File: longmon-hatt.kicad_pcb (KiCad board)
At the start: 2 copper layers, 2 parts

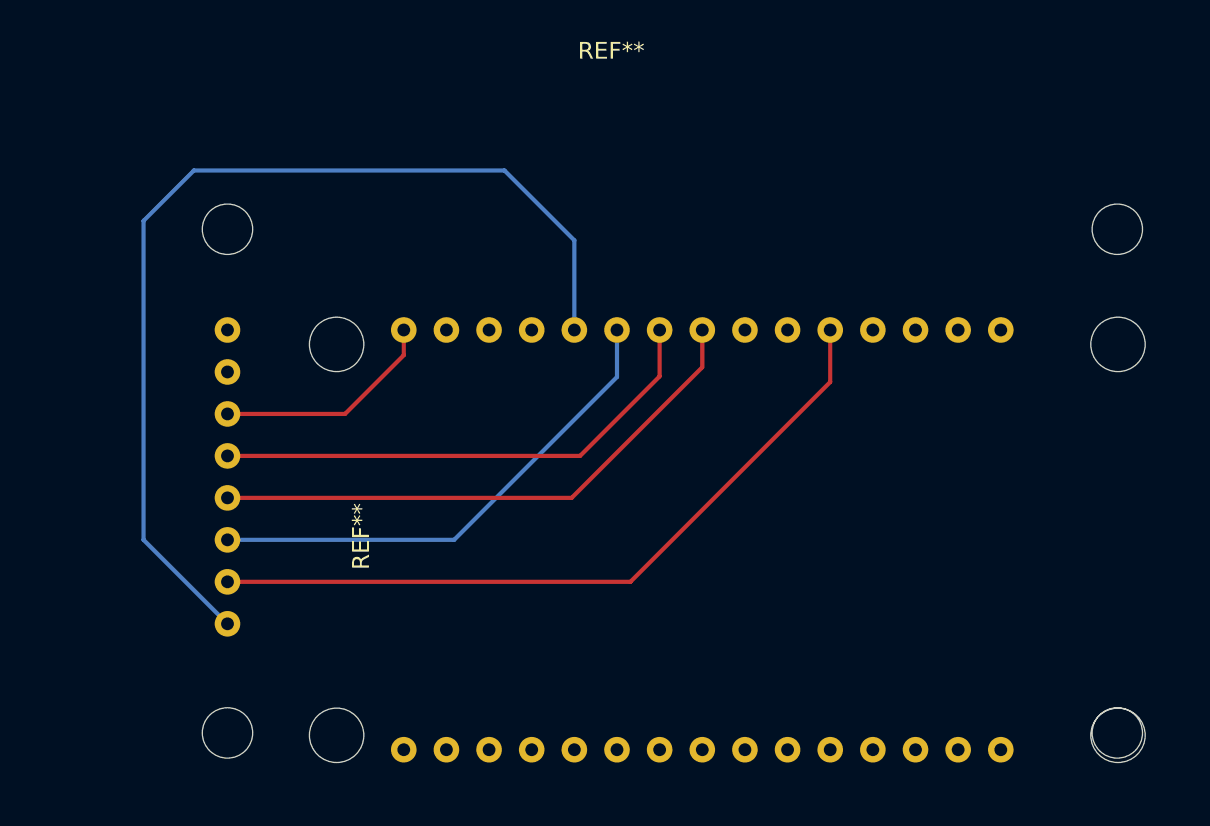
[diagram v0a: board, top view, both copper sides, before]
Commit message: Fixed pad numbers on ESP footprint, fix ref designators on PCB
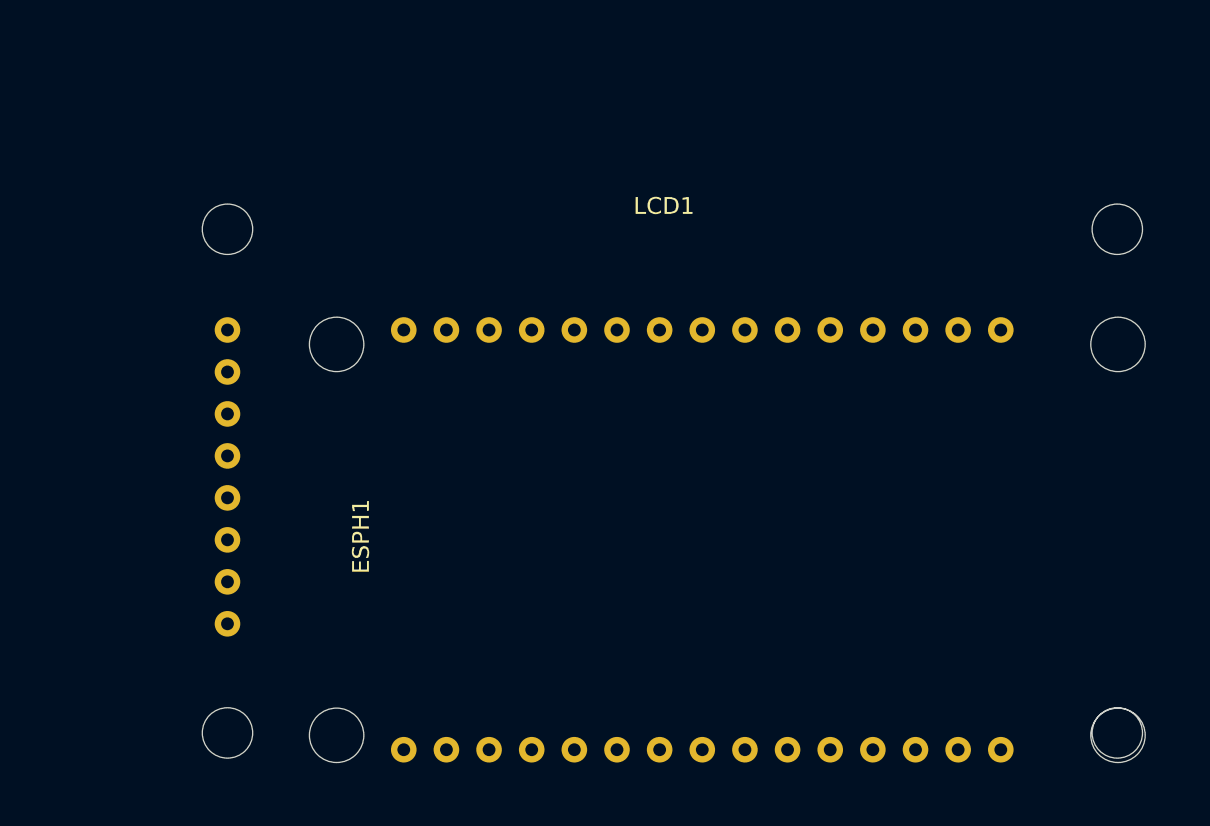
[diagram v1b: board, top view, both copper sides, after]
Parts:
- ESPH1: renamed from REF**; value ESP_Header -> ~
- LCD1: renamed from REF**; value LCD Module -> ~
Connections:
- ESPH1 pad 10: (no net) -> Net-(ESPH1-D34)
- ESPH1 pad 11: (no net) -> unconnected-(ESPH1-D35-Pad11)
- ESPH1 pad 12: (no net) -> unconnected-(ESPH1-D32-Pad12)
- ESPH1 pad 13: (no net) -> unconnected-(ESPH1-D33-Pad13)
- ESPH1 pad 14: (no net) -> unconnected-(ESPH1-D25-Pad14)
- ESPH1 pad 15: (no net) -> unconnected-(ESPH1-D26-Pad15)
- ESPH1 pad 16: (no net) -> unconnected-(ESPH1-D27-Pad16)
- ESPH1 pad 17: (no net) -> unconnected-(ESPH1-D14-Pad17)
- ESPH1 pad 18: (no net) -> unconnected-(ESPH1-D12-Pad18)
- ESPH1 pad 20: (no net) -> unconnected-(ESPH1-D13-Pad20)
- ESPH1 pad 21: (no net) -> unconnected-(ESPH1-D15-Pad21)
- ESPH1 pad 22: (no net) -> unconnected-(ESPH1-D2-Pad22)
- ESPH1 pad 24: (no net) -> Net-(ESPH1-D4)
- ESPH1 pad 25: (no net) -> Net-(ESPH1-RX2)
- ESPH1 pad 27: (no net) -> Net-(ESPH1-TX2)
- ESPH1 pad 5: (no net) -> unconnected-(ESPH1-VP-Pad5)
- ESPH1 pad 8: (no net) -> unconnected-(ESPH1-VN-Pad8)
- ESPH1 pad 9: (no net) -> unconnected-(ESPH1-EN-Pad9)
- LCD1 pad 1: (no net) -> Net-(LCD1-VCC)
- LCD1 pad 2: (no net) -> Net-(LCD1-GND)
- LCD1 pad 3: (no net) -> Net-(ESPH1-D23)
- LCD1 pad 4: (no net) -> Net-(ESPH1-D18)
- LCD1 pad 5: (no net) -> Net-(ESPH1-D5)
- LCD1 pad 6: (no net) -> Net-(ESPH1-D19)
- LCD1 pad 7: (no net) -> Net-(ESPH1-D4)
- LCD1 pad 8: (no net) -> Net-(ESPH1-D21)
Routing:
- net (no net): track 211.6 -> 0.00 mm

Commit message: Add LoRa header (TODO: fix pin order), add edge cut
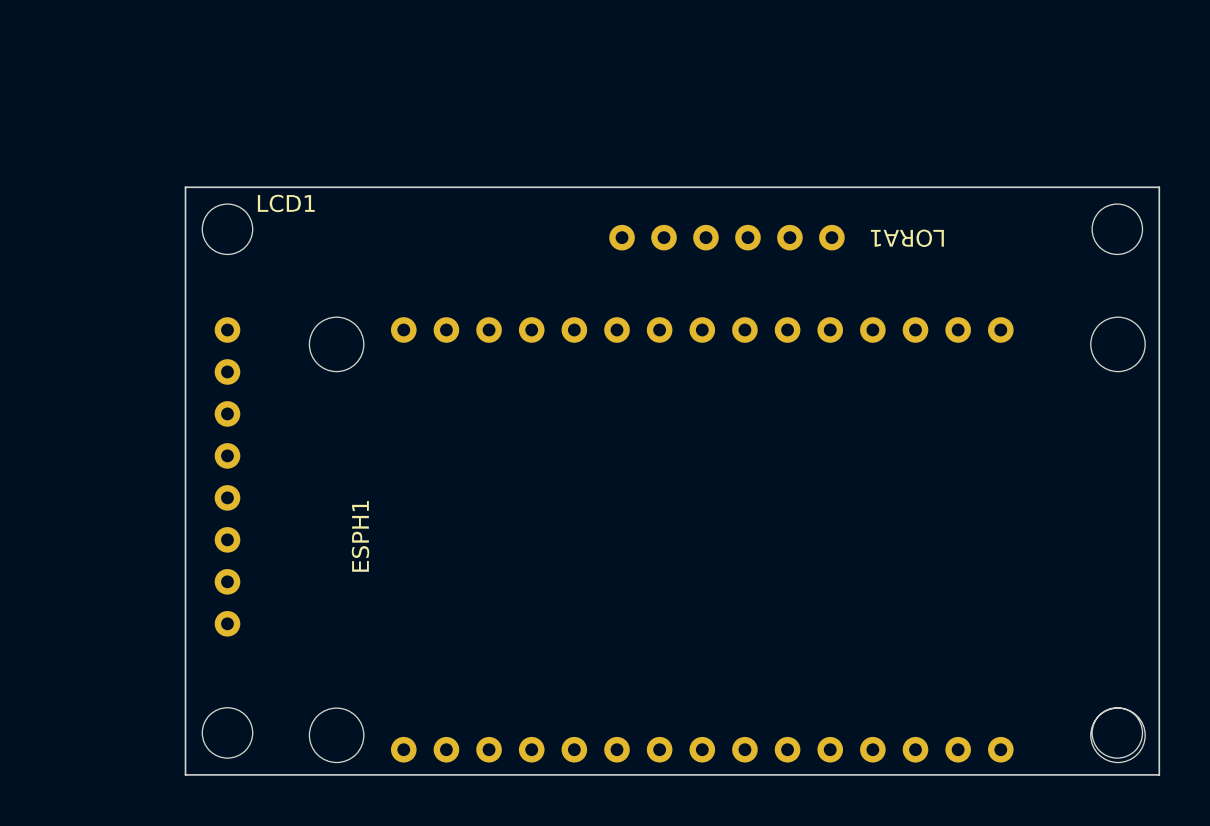
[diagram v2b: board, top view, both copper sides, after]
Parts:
- added LORA1: ~, ESP:LoRa Header, F.Cu at (175.5, 82.0)
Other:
- board outline added: 58 x 35 mm
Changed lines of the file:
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@@
     )
     (pad_to_mask_clearance 0)
+    (aux_axis_origin 166 96.5)
     (pcbplotparams
       (layerselection 0x00010fc_ffffffff)
@@
   (net 28 "Net-(LCD1-GND)")
   (net 29 "Net-(ESPH1-PadVIN)")
+  (net 30 "unconnected-(LORA1-NRST-Pad4)")
   (footprint "ESP:ESP_Header" (layer "F.Cu")
     (at 150 112.5 90)
@@
         (effects (font (size 1 1) (thickness 0.1)))
     )
-    (fp_text value "~" (at 12.7 0 90 unlocked) (layer "F.Fab")
+    (fp_text value "~" (at 12.7 0 90 unlocked) (layer "F.Fab") hide
         (effects (font (size 1 1) (thickness 0.15)))
     )
@@
       (net 29 "Net-(ESPH1-PadVIN)") (pinfunction "VIN") (pintype "power_in"))
   )
+  (footprint "ESP:LoRa Header" (layer "F.Cu")
+    (at 175.5 82 -90)
+    (property "Sheetfile" "longmon-hatt.kicad_sch")
+    (property "Sheetname" "")
+    (property "Sim.Enable" "0")
+    (attr through_hole)
+    (fp_text reference "LORA1" (at 0 -4.5 -180 unlocked) (layer "F.SilkS")
+        (effects (font (size 1 1) (thickness 0.1)))
+    )
+    (fp_text value "~" (at 12.5 -5 -90 unlocked) (layer "F.Fab") hide
+        (effects (font (size 1 1) (thickness 0.15)))
+    )
+    (fp_text user "${REFERENCE}" (at 12.5 -3.5 -90 unlocked) (layer "F.Fab") hide
+        (effects (font (size 1 1) (thickness 0.15)))
+    )
+    (pad "1" thru_hole circle (at 0 0 270) (size 1.524 1.524) (drill 0.762) (layers "*.Cu" "*.Mask")
+      (net 28 "Net-(LCD1-GND)") (pinfunction "GND") (pintype "power_in"))
+    (pad "2" thru_hole circle (at 0 2.5 270) (size 1.524 1.524) (drill 0.762) (layers "*.Cu" "*.Mask")
+      (net 18 "Net-(ESPH1-RX2)") (pinfunction "TXD") (pintype "output"))
+    (pad "3" thru_hole circle (at 0 5 270) (size 1.524 1.524) (drill 0.762) (layers "*.Cu" "*.Mask")
+      (net 19 "Net-(ESPH1-TX2)") (pinfunction "RXD") (pintype "input"))
+    (pad "4" thru_hole circle (at 0 7.5 270) (size 1.524 1.524) (drill 0.762) (layers "*.Cu" "*.Mask")
+      (net 30 "unconnected-(LORA1-NRST-Pad4)") (pinfunction "NRST") (pintype "no_connect"))
+    (pad "5" thru_hole circle (at 0 10 270) (size 1.524 1.524) (drill 0.762) (layers "*.Cu" "*.Mask")
+      (net 1 "Net-(LCD1-VCC)") (pinfunction "VDD") (pintype "power_in"))
+    (pad "6" thru_hole circle (at 0 12.5 270) (size 1.524 1.524) (drill 0.762) (layers "*.Cu" "*.Mask"))
+  )
   (footprint "ESP:LCD Module" (layer "F.Cu")
     (at 139.5 81.5)
@@
     (property "Sim.Enable" "0")
     (attr through_hole)
-    (fp_text reference "LCD1" (at 26 -1.38 unlocked) (layer "F.SilkS")
+    (fp_text reference "LCD1" (at 3.5 -1.5 unlocked) (layer "F.SilkS")
         (effects (font (size 1 1) (thickness 0.1)))
     )
-    (fp_text value "~" (at 26 0.5 unlocked) (layer "F.Fab")
+    (fp_text value "~" (at 26 0.5 unlocked) (layer "F.Fab") hide
         (effects (font (size 1 1) (thickness 0.15)))
     )
@@
       (net 27 "Net-(ESPH1-D21)") (pinfunction "BL") (pintype "input"))
   )
+  (gr_rect (start 137 79) (end 195 114)
+    (stroke (width 0.1) (type default)) (fill none) (layer "Edge.Cuts"))
 )

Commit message: Fix LoRa pins and pads, add design constraints
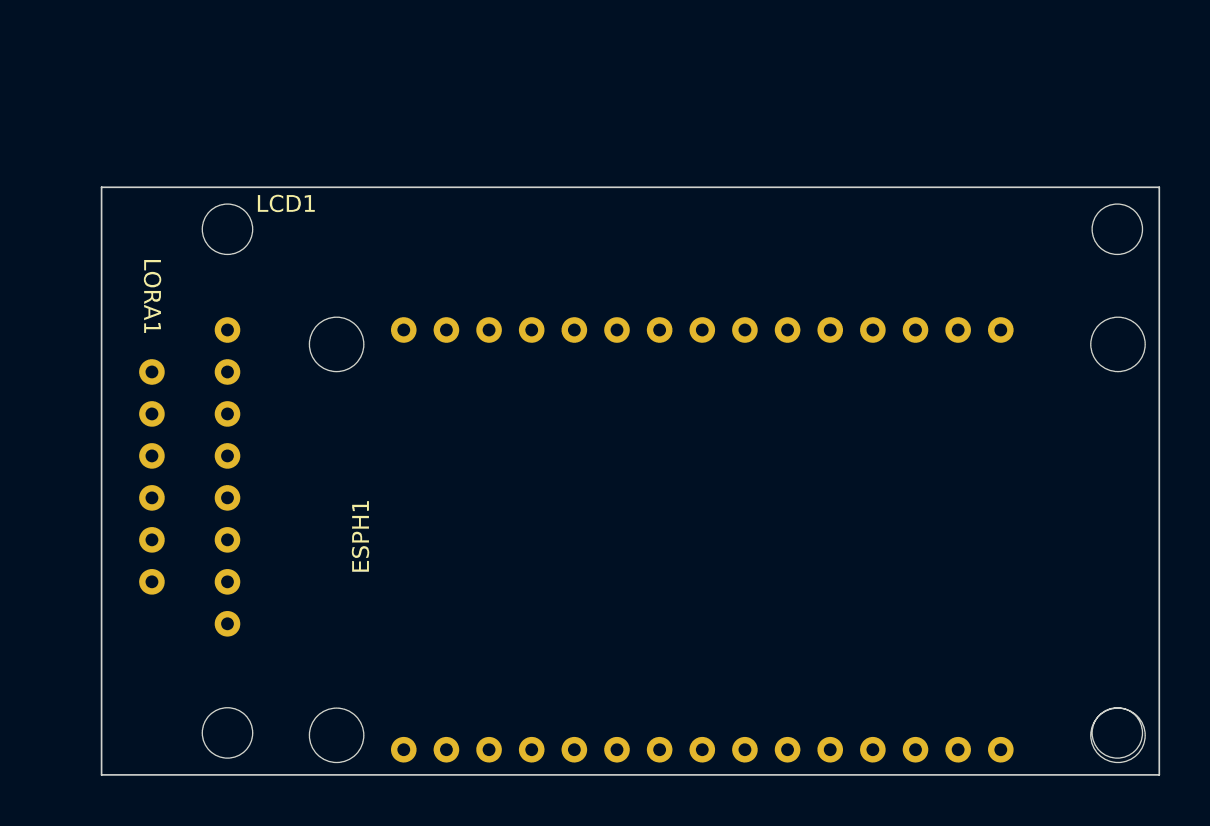
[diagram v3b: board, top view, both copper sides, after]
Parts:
- moved LORA1 41.3 mm to (135.0, 90.0), turned to 0 degrees
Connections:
- LORA1 pad 2: Net-(ESPH1-RX2) -> (no net)
- LORA1 pad 3: Net-(ESPH1-TX2) -> Net-(ESPH1-RX2)
- LORA1 pad 4: unconnected-(LORA1-NRST-Pad4) -> Net-(ESPH1-TX2)
- LORA1 pad 5: Net-(LCD1-VCC) -> unconnected-(LORA1-NRST-Pad5)
- LORA1 pad 6: (no net) -> Net-(LCD1-VCC)
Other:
- board size 58 x 35 mm -> 63 x 35 mm
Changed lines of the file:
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@@
   (net 28 "Net-(LCD1-GND)")
   (net 29 "Net-(ESPH1-PadVIN)")
-  (net 30 "unconnected-(LORA1-NRST-Pad4)")
+  (net 30 "unconnected-(LORA1-NRST-Pad5)")
   (footprint "ESP:ESP_Header" (layer "F.Cu")
     (at 150 112.5 90)
@@
   )
   (footprint "ESP:LoRa Header" (layer "F.Cu")
-    (at 175.5 82 -90)
+    (at 135 90)
     (property "Sheetfile" "longmon-hatt.kicad_sch")
     (property "Sheetname" "")
     (property "Sim.Enable" "0")
     (attr through_hole)
-    (fp_text reference "LORA1" (at 0 -4.5 -180 unlocked) (layer "F.SilkS")
+    (fp_text reference "LORA1" (at 0 -4.5 -90 unlocked) (layer "F.SilkS")
         (effects (font (size 1 1) (thickness 0.1)))
     )
-    (fp_text value "~" (at 12.5 -5 -90 unlocked) (layer "F.Fab") hide
+    (fp_text value "~" (at 12.5 -5 unlocked) (layer "F.Fab") hide
         (effects (font (size 1 1) (thickness 0.15)))
     )
-    (fp_text user "${REFERENCE}" (at 12.5 -3.5 -90 unlocked) (layer "F.Fab") hide
+    (fp_text user "${REFERENCE}" (at 12.5 -3.5 unlocked) (layer "F.Fab") hide
         (effects (font (size 1 1) (thickness 0.15)))
     )
-    (pad "1" thru_hole circle (at 0 0 270) (size 1.524 1.524) (drill 0.762) (layers "*.Cu" "*.Mask")
+    (pad "1" thru_hole circle (at 0 0) (size 1.524 1.524) (drill 0.762) (layers "*.Cu" "*.Mask")
       (net 28 "Net-(LCD1-GND)") (pinfunction "GND") (pintype "power_in"))
-    (pad "2" thru_hole circle (at 0 2.5 270) (size 1.524 1.524) (drill 0.762) (layers "*.Cu" "*.Mask")
+    (pad "2" thru_hole circle (at 0 2.5) (size 1.524 1.524) (drill 0.762) (layers "*.Cu" "*.Mask"))
+    (pad "3" thru_hole circle (at 0 5) (size 1.524 1.524) (drill 0.762) (layers "*.Cu" "*.Mask")
       (net 18 "Net-(ESPH1-RX2)") (pinfunction "TXD") (pintype "output"))
-    (pad "3" thru_hole circle (at 0 5 270) (size 1.524 1.524) (drill 0.762) (layers "*.Cu" "*.Mask")
+    (pad "4" thru_hole circle (at 0 7.5) (size 1.524 1.524) (drill 0.762) (layers "*.Cu" "*.Mask")
       (net 19 "Net-(ESPH1-TX2)") (pinfunction "RXD") (pintype "input"))
-    (pad "4" thru_hole circle (at 0 7.5 270) (size 1.524 1.524) (drill 0.762) (layers "*.Cu" "*.Mask")
-      (net 30 "unconnected-(LORA1-NRST-Pad4)") (pinfunction "NRST") (pintype "no_connect"))
-    (pad "5" thru_hole circle (at 0 10 270) (size 1.524 1.524) (drill 0.762) (layers "*.Cu" "*.Mask")
+    (pad "5" thru_hole circle (at 0 10) (size 1.524 1.524) (drill 0.762) (layers "*.Cu" "*.Mask")
+      (net 30 "unconnected-(LORA1-NRST-Pad5)") (pinfunction "NRST") (pintype "no_connect"))
+    (pad "6" thru_hole circle (at 0 12.5) (size 1.524 1.524) (drill 0.762) (layers "*.Cu" "*.Mask")
       (net 1 "Net-(LCD1-VCC)") (pinfunction "VDD") (pintype "power_in"))
-    (pad "6" thru_hole circle (at 0 12.5 270) (size 1.524 1.524) (drill 0.762) (layers "*.Cu" "*.Mask"))
   )
   (footprint "ESP:LCD Module" (layer "F.Cu")
@@
       (net 27 "Net-(ESPH1-D21)") (pinfunction "BL") (pintype "input"))
   )
-  (gr_rect (start 137 79) (end 195 114)
+  (gr_rect (start 132 79) (end 195 114)
     (stroke (width 0.1) (type default)) (fill none) (layer "Edge.Cuts"))
 )

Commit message: Add POT header
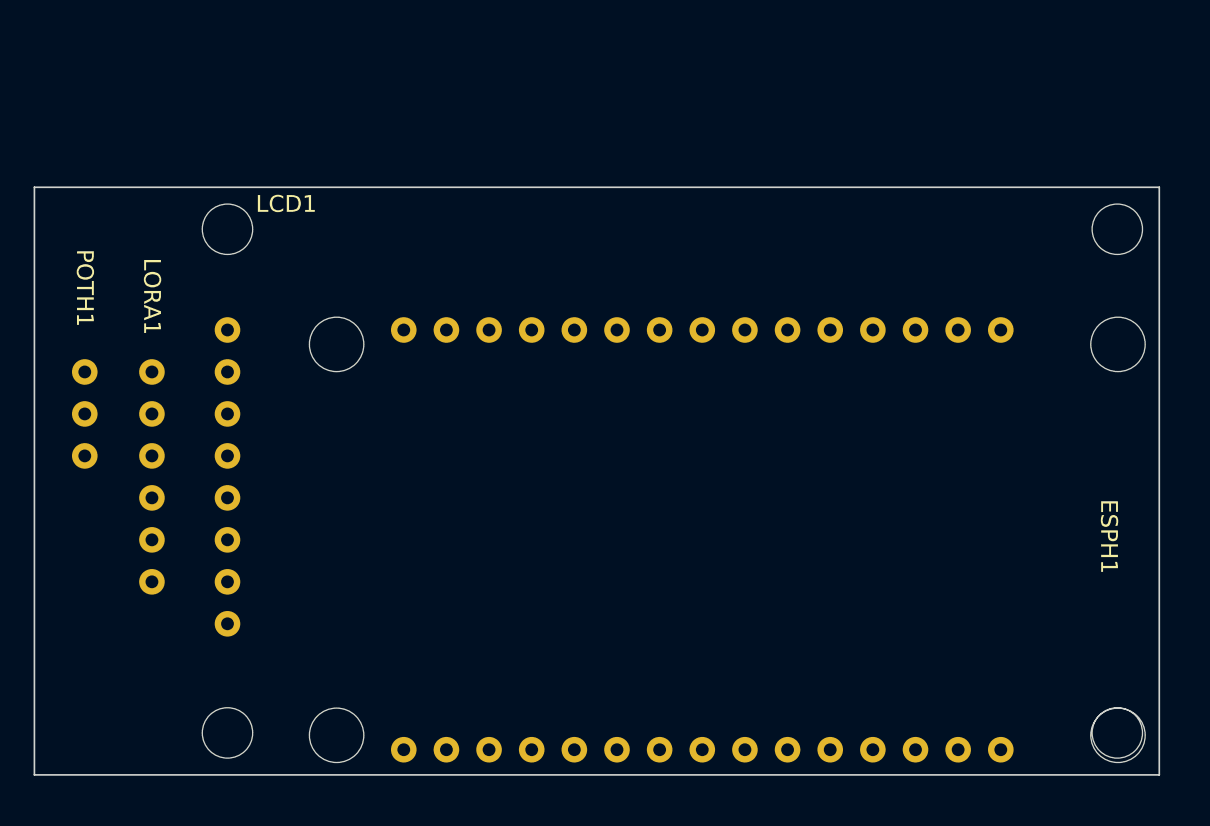
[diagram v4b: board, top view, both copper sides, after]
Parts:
- added POTH1: ~, ESP:POT Header, F.Cu at (131.0, 90.0)
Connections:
- ESPH1 pad VIN: Net-(ESPH1-PadVIN) -> unconnected-(ESPH1-PadVIN)
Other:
- board size 63 x 35 mm -> 67 x 35 mm
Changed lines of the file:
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@@
   (net 27 "Net-(ESPH1-D21)")
   (net 28 "Net-(LCD1-GND)")
-  (net 29 "Net-(ESPH1-PadVIN)")
+  (net 29 "unconnected-(ESPH1-PadVIN)")
   (net 30 "unconnected-(LORA1-NRST-Pad5)")
   (footprint "ESP:ESP_Header" (layer "F.Cu")
@@
     (property "ki_keywords" "ESP, header")
     (attr through_hole)
-    (fp_text reference "ESPH1" (at 12.7 -2.54 90 unlocked) (layer "F.SilkS")
+    (fp_text reference "ESPH1" (at 12.7 42 270 unlocked) (layer "F.SilkS")
         (effects (font (size 1 1) (thickness 0.1)))
     )
@@
       (net 28 "Net-(LCD1-GND)") (pinfunction "GND") (pintype "power_in"))
     (pad "VIN" thru_hole circle (at 0 35.56 90) (size 1.524 1.524) (drill 0.762) (layers "*.Cu" "*.Mask")
-      (net 29 "Net-(ESPH1-PadVIN)") (pinfunction "VIN") (pintype "power_in"))
+      (net 29 "unconnected-(ESPH1-PadVIN)") (pinfunction "VIN") (pintype "power_in"))
   )
   (footprint "ESP:LoRa Header" (layer "F.Cu")
@@
       (net 1 "Net-(LCD1-VCC)") (pinfunction "VDD") (pintype "power_in"))
   )
+  (footprint "ESP:POT Header" (layer "F.Cu")
+    (at 131 90)
+    (property "Sheetfile" "longmon-hatt.kicad_sch")
+    (property "Sheetname" "")
+    (property "Sim.Enable" "0")
+    (attr through_hole)
+    (fp_text reference "POTH1" (at 0 -5 -90 unlocked) (layer "F.SilkS")
+        (effects (font (size 1 1) (thickness 0.1)))
+    )
+    (fp_text value "~" (at 7.5 1.5 unlocked) (layer "F.Fab") hide
+        (effects (font (size 1 1) (thickness 0.15)))
+    )
+    (fp_text user "${REFERENCE}" (at 7.5 3 unlocked) (layer "F.Fab") hide
+        (effects (font (size 1 1) (thickness 0.15)))
+    )
+    (pad "DIV" thru_hole circle (at 0 2.5) (size 1.524 1.524) (drill 0.762) (layers "*.Cu" "*.Mask")
+      (net 5 "Net-(ESPH1-D34)") (pinfunction "DIV") (pintype "output"))
+    (pad "GND" thru_hole circle (at 0 5) (size 1.524 1.524) (drill 0.762) (layers "*.Cu" "*.Mask")
+      (net 28 "Net-(LCD1-GND)") (pinfunction "GND") (pintype "power_in"))
+    (pad "VCC" thru_hole circle (at 0 0) (size 1.524 1.524) (drill 0.762) (layers "*.Cu" "*.Mask")
+      (net 1 "Net-(LCD1-VCC)") (pinfunction "VCC") (pintype "power_in"))
+  )
   (footprint "ESP:LCD Module" (layer "F.Cu")
     (at 139.5 81.5)
@@
       (net 27 "Net-(ESPH1-D21)") (pinfunction "BL") (pintype "input"))
   )
-  (gr_rect (start 132 79) (end 195 114)
+  (gr_rect (start 128 79) (end 195 114)
     (stroke (width 0.1) (type default)) (fill none) (layer "Edge.Cuts"))
 )
